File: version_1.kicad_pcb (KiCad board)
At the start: 2 copper layers, 98.6 x 99.9 mm, 145 parts, among them J1 motor_connector, J2 motor_connector, J3 motor_connector, J4 motor_connector, M5 Motor_Servo_JR, M6 Motor_Servo_JR, M7 Motor_Servo_JR, M8 Motor_Servo_JR, Q1 AO3400A, Q10 AO3400A, Q11 AO3400A, Q12 AO3400A, Q13 AO3400A, Q14 AO3400A, Q15 AO3400A, Q16 AO3400A, Q17 AO3401A, Q18 AO3401A, Q19 AO3401A, Q2 AO3400A, Q20 AO3401A, Q21 AO3400A, Q22 AO3400A, Q23 AO3400A, Q24 AO3400A, Q25 AO3400A, Q26 AO3400A, Q3 AO3400A, Q4 AO3400A, Q5 AO3400A, Q6 AO3400A, Q7 AO3400A, Q8 AO3400A, Q9 AO3400A, SW1 SW_SPDT, U1 Pico, U10 74AHC595, U11 ADP2302ARDZ-5.0, U12 LSM6DS3, U2 SLM2009, U3 SLM2009, U4 SLM2009, U5 SLM2009, U6 SLM2009, U7 SLM2009, U8 SLM2009, U9 SLM2009

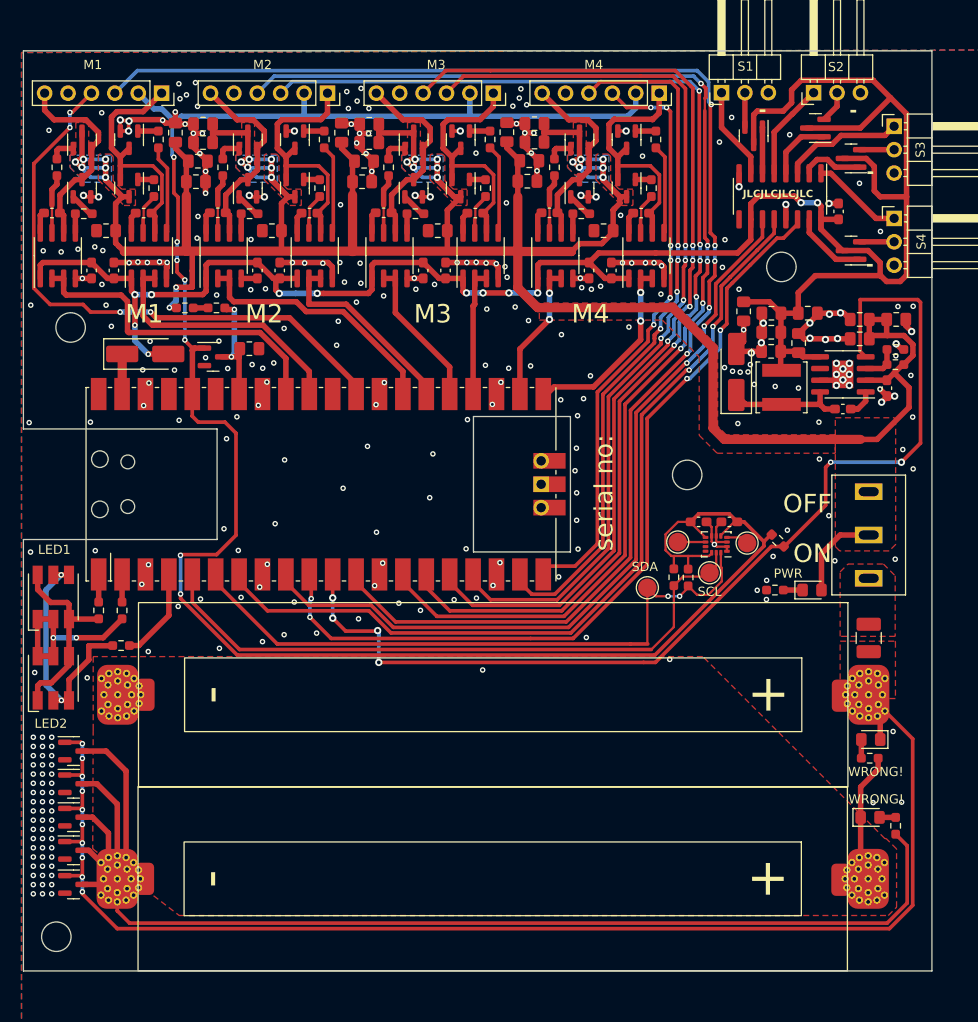
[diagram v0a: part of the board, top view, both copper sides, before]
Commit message: new version of layout with diodes improved power routing a little bit
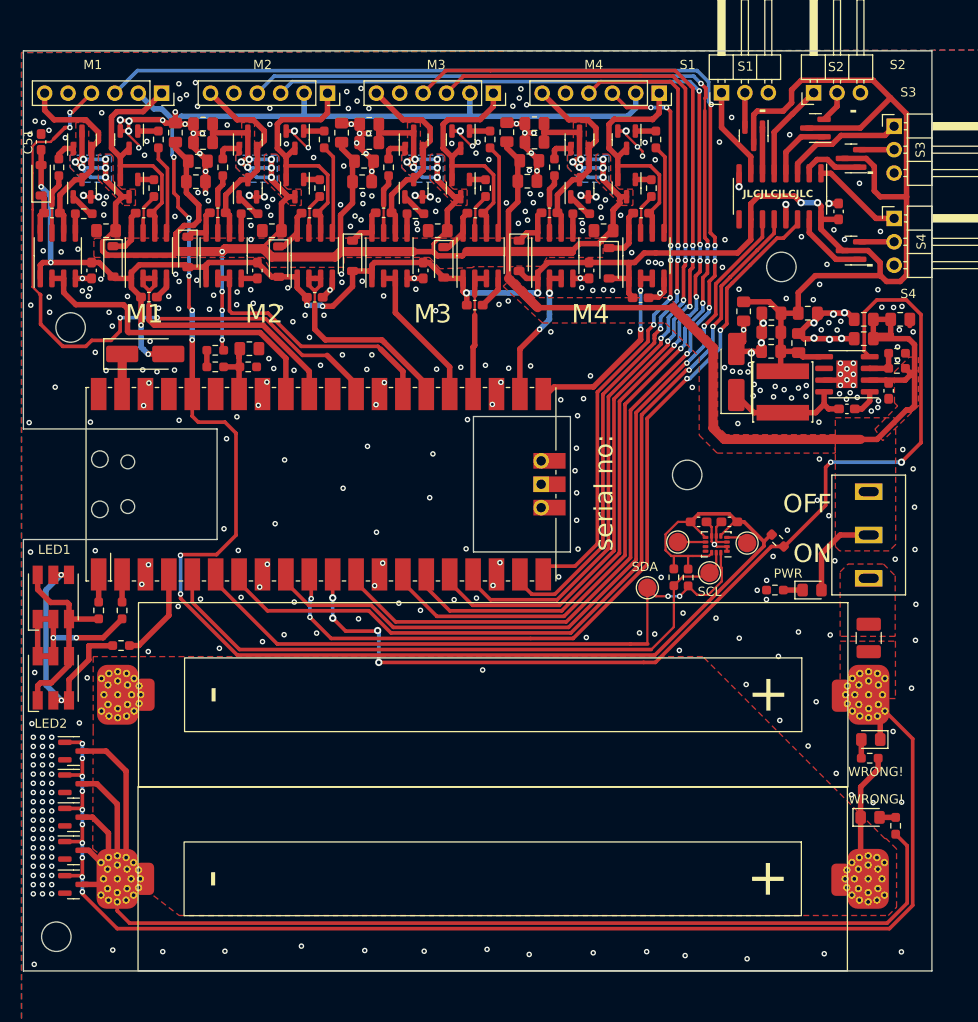
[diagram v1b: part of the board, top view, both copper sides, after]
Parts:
- removed Q26: AO3400A, Package_TO_SOT_SMD:SOT-23
- added C51: 100n, Capacitor_SMD:C_0603_1608Metric_Pad1.08x0.95mm_HandSolder, F.Cu at (25.6, 31.3)
- added D10: C8598, Diode_SMD:D_SOD-123, F.Cu at (77.4, 43.6)
- added D11: C8598, Diode_SMD:D_SOD-123, F.Cu at (25.6, 35.5)
- added D12: C8598, Diode_SMD:D_SOD-123, F.Cu at (51.3, 44.3)
- added D13: C8598, Diode_SMD:D_SOD-123, F.Cu at (69.2, 44.4)
- added D14: C8598, Diode_SMD:D_SOD-123, F.Cu at (87.2, 44.5)
- added D15: C8598, Diode_SMD:D_SOD-123, F.Cu at (33.4, 44.2)
- added D8: C8598, Diode_SMD:D_SOD-123, F.Cu at (41.5, 43.2)
- added D9: C8598, Diode_SMD:D_SOD-123, F.Cu at (59.4, 43.6)
- added R25: 1k, Resistor_SMD:R_0603_1608Metric_Pad0.98x0.95mm_HandSolder, F.Cu at (48.0, 55.7)
- L1: footprint Inductor_SMD:L_Changjiang_FNR5020S -> Inductor_SMD:L_Changjiang_FNR6045S
- moved R26 6.40 mm to (44.5, 55.7)
- moved R27 5.66 mm to (44.5, 53.9), turned to 180 degrees
- moved C22 4.92 mm to (72.6, 49.0), turned to 0 degrees
- moved C21 4.79 mm to (55.2, 48.1), turned to 0 degrees
- moved C24 4.78 mm to (37.2, 48.1), turned to 0 degrees
- moved C23 4.34 mm to (90.6, 48.2), turned to 0 degrees
- moved L1 0.52 mm to (106.0, 58.4)
- moved R18 0.44 mm to (118.5, 54.2)
- moved R19 0.44 mm to (118.5, 55.9)
- moved C13 0.44 mm to (118.8, 50.5)
- moved C30 0.44 mm to (114.8, 52.6)
- moved C31 0.44 mm to (114.8, 50.5)
- moved U11 0.44 mm to (113.0, 56.5)
- moved C9 0.44 mm to (113.0, 60.3)
- moved C14 0.34 mm to (117.5, 58.3)
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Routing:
- net VCC: track 409.0 -> 362.1 mm, vias 26 -> 28
- net +5V: track 232.6 -> 249.1 mm, vias 12 -> 10
- net GND: track 138.8 -> 125.4 mm, vias 305 -> 424
- net /ENCODER7: track 65.2 -> 71.7 mm
- net Net-(U1-GPIO28_ADC2): track 14.2 -> 7.66 mm, vias 2 -> 0
- net Net-(D14-K): track 2.33 -> 5.83 mm
- net Net-(D15-K): track 2.33 -> 5.37 mm
- net /MR1: track 22.3 -> 25.2 mm
- net Net-(D13-K): track 2.33 -> 5.07 mm
- net Net-(D12-K): track 2.33 -> 4.97 mm
- net Net-(D9-K): track 2.48 -> 4.93 mm
- net Net-(D10-K): track 2.48 -> 4.86 mm
- net Net-(D8-K): track 2.48 -> 4.63 mm
- net Net-(D11-K): track 2.48 -> 4.51 mm
- net /power/Pgood: track 114.8 -> 112.8 mm
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
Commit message: najnowsza wersja
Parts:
- removed D7: C2843868, LED_SMD:LED_RGB_5050-6
- U12: value LSM6DS3 -> C967633
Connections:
- D6 pad 1: Net-(D6-BA) -> GND
- D6 pad 2: Net-(D6-BK) -> GND
- D6 pad 3: Net-(D6-BK) -> GND
- D6 pad 6: Net-(D6-GA) -> Net-(D6-RA)
- R21 pad 1: Net-(D6-BA) -> Net-(D6-RA)
- R23 pad 1: Net-(D6-BK) -> Net-(D6-BA)
- R23 pad 2: Net-(U1-GPIO2) -> Net-(U1-GPIO4)
- U1 pad 4: Net-(U1-GPIO2) -> /SDA
- U1 pad 6: /SDA -> Net-(U1-GPIO4)
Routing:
- net Net-(D6-BK): track 27.8 -> 0.00 mm, vias 2 -> 0
- net Net-(U1-GPIO4): track 0.00 -> 17.7 mm, vias 0 -> 2
- net Net-(D6-BA): track 21.4 -> 5.21 mm
- net Net-(U1-GPIO2): track 11.0 -> 0.00 mm
- net Net-(D6-GA): track 19.8 -> 9.81 mm, vias 2 -> 0
- net Net-(D6-RA): track 0.00 -> 9.23 mm
- net /SDA: track 70.8 -> 78.7 mm, vias 2 -> 4
- net GND: vias 424 -> 431

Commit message: added moany componaets
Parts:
- added C11: 22u, Capacitor_SMD:C_0805_2012Metric_Pad1.18x1.45mm_HandSolder, F.Cu at (169.6, 102.1)
- added C32: 22u, Capacitor_SMD:C_0805_2012Metric_Pad1.18x1.45mm_HandSolder, F.Cu at (169.6, 105.1)
- added C33: 22u, Capacitor_SMD:C_0805_2012Metric_Pad1.18x1.45mm_HandSolder, F.Cu at (169.6, 108.1)
- added C34: 22u, Capacitor_SMD:C_0805_2012Metric_Pad1.18x1.45mm_HandSolder, F.Cu at (169.6, 111.1)
- added C35: 22u, Capacitor_SMD:C_0805_2012Metric_Pad1.18x1.45mm_HandSolder, F.Cu at (169.6, 114.1)
- added C40: 22u, Capacitor_SMD:C_0805_2012Metric_Pad1.18x1.45mm_HandSolder, F.Cu at (185.9, 102.1)
- added C41: 22u, Capacitor_SMD:C_0805_2012Metric_Pad1.18x1.45mm_HandSolder, F.Cu at (197.8, 91.5)
- added C42: 22u, Capacitor_SMD:C_0805_2012Metric_Pad1.18x1.45mm_HandSolder, F.Cu at (197.8, 94.5)
- added C43: 22u, Capacitor_SMD:C_0805_2012Metric_Pad1.18x1.45mm_HandSolder, F.Cu at (197.8, 97.5)
- added C44: 22u, Capacitor_SMD:C_0805_2012Metric_Pad1.18x1.45mm_HandSolder, F.Cu at (185.9, 114.1)
- added C45: 22u, Capacitor_SMD:C_0805_2012Metric_Pad1.18x1.45mm_HandSolder, F.Cu at (197.8, 71.5)
- added C46: 22u, Capacitor_SMD:C_0805_2012Metric_Pad1.18x1.45mm_HandSolder, F.Cu at (197.8, 74.5)
- added C47: 22u, Capacitor_SMD:C_0805_2012Metric_Pad1.18x1.45mm_HandSolder, F.Cu at (185.9, 91.1)
- added C48: 22u, Capacitor_SMD:C_0805_2012Metric_Pad1.18x1.45mm_HandSolder, F.Cu at (185.9, 94.1)
- added C49: 22u, Capacitor_SMD:C_0805_2012Metric_Pad1.18x1.45mm_HandSolder, F.Cu at (185.9, 97.1)
- added C52: 22u, Capacitor_SMD:C_0805_2012Metric_Pad1.18x1.45mm_HandSolder, F.Cu at (169.6, 85.1)
- added C53: 22u, Capacitor_SMD:C_0805_2012Metric_Pad1.18x1.45mm_HandSolder, F.Cu at (169.6, 88.1)
- added C54: 22u, Capacitor_SMD:C_0805_2012Metric_Pad1.18x1.45mm_HandSolder, F.Cu at (169.6, 91.1)
- added C55: 22u, Capacitor_SMD:C_0805_2012Metric_Pad1.18x1.45mm_HandSolder, F.Cu at (169.6, 94.1)
- added C56: 22u, Capacitor_SMD:C_0805_2012Metric_Pad1.18x1.45mm_HandSolder, F.Cu at (169.6, 97.1)
- added CN1: B6B-PH-K-S(LF)(SN), footprint:CONN-TH_B6B-PH-K-S, F.Cu at (190.0, 134.5)
- added CN2: B6B-PH-K-S(LF)(SN), footprint:CONN-TH_B6B-PH-K-S, F.Cu at (207.3, 134.5)
- added CN3: B6B-PH-K-S(LF)(SN), footprint:CONN-TH_B6B-PH-K-S, F.Cu at (172.7, 134.5)
- added CN4: B6B-PH-K-S(LF)(SN), footprint:CONN-TH_B6B-PH-K-S, F.Cu at (155.4, 134.5)
- added U13: DRV8870DDA, Package_SO:Texas_HTSOP-8-1EP_3.9x4.9mm_P1.27mm_EP2.95x4.9mm_Mask2.4x3.1mm_ThermalVias, F.Cu at (177.5, 70.5)
- added U14: BH-18650-B5BA016, footprint:BAT-SMD_BH-18650-B5BA016, F.Cu at (74.6, 111.3)
- added U15: DRV8870DDA, Package_SO:Texas_HTSOP-8-1EP_3.9x4.9mm_P1.27mm_EP2.95x4.9mm_Mask2.4x3.1mm_ThermalVias, F.Cu at (168.8, 58.3)
- added U16: DRV8870DDA, Package_SO:Texas_HTSOP-8-1EP_3.9x4.9mm_P1.27mm_EP2.95x4.9mm_Mask2.4x3.1mm_ThermalVias, F.Cu at (179.0, 47.6)
- added U17: DRV8870DDA, Package_SO:Texas_HTSOP-8-1EP_3.9x4.9mm_P1.27mm_EP2.95x4.9mm_Mask2.4x3.1mm_ThermalVias, F.Cu at (195.2, 57.3)
- R25: value 1k -> 10k
- R26: value 1k -> 33k
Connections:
- R26 pad 1: Net-(R26-Pad1) -> VCC
- U1 pad 11: /power/Pgood -> /ENCODER7
- U1 pad 29: /ENCODER7 -> /power/Pgood

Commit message: specified correct shift register
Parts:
- added C1: 100n, Capacitor_SMD:C_0603_1608Metric_Pad1.08x0.95mm_HandSolder, F.Cu at (160.8, 38.3)
- added C2: 100n, Capacitor_SMD:C_0603_1608Metric_Pad1.08x0.95mm_HandSolder, F.Cu at (132.7, 105.2)
- added C3: 100n, Capacitor_SMD:C_0603_1608Metric_Pad1.08x0.95mm_HandSolder, F.Cu at (160.8, 33.8)
- added C4: 100n, Capacitor_SMD:C_0603_1608Metric_Pad1.08x0.95mm_HandSolder, F.Cu at (160.8, 29.3)
- added D1: WRONG!, Diode_SMD:D_0805_2012Metric_Pad1.15x1.40mm_HandSolder, F.Cu at (133.0, 94.3)
- added D3: WRONG!, Diode_SMD:D_0805_2012Metric_Pad1.15x1.40mm_HandSolder, F.Cu at (133.0, 97.3)
- added D7: WRONG!, Diode_SMD:D_0805_2012Metric_Pad1.15x1.40mm_HandSolder, F.Cu at (133.0, 100.4)
- added F1: DFN, Fuse:Fuse_1210_3225Metric_Pad1.42x2.65mm_HandSolder, F.Cu at (142.7, 94.9)
- added R17: 1k, Resistor_SMD:R_0603_1608Metric_Pad0.98x0.95mm_HandSolder, F.Cu at (137.5, 94.0)
- added R20: 1k, Resistor_SMD:R_0603_1608Metric_Pad0.98x0.95mm_HandSolder, F.Cu at (137.5, 96.5)
- added R27: 1k, Resistor_SMD:R_0603_1608Metric_Pad0.98x0.95mm_HandSolder, F.Cu at (137.5, 99.1)
- added U18: SM04B-SRSS-TB_(LF)(SN), footprint:CONN-SMD_4P-P1.00_SM04B-SRSS-TB-LF-SN, F.Cu at (141.1, 59.4)
- added U2: SS-12D10L5, footprint:SW-TH_SS-12D10L5, F.Cu at (128.3, 73.3)
- M5, M6, M7, M8: footprint Connector_PinHeader_2.54mm:PinHeader_1x03_P2.54mm_Horizontal -> Connector_PinHeader_2.54mm:PinHeader_1x03_P2.54mm_Vertical
- moved U14 53.4 mm to (72.9, 164.6)
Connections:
- net /Untitled Sheet5/PWM renamed /Servo2/PWM
- net /Untitled Sheet5/PWR renamed /Servo2/PWR
- net /Untitled Sheet6/PWM renamed /Servo/PWM
- net /Untitled Sheet6/PWR renamed /Servo/PWR
- net /power/Pgood renamed /Power/Pgood
- CN1 pad 2: unconnected-(CN1-Pad2) -> GND
- CN1 pad 3: unconnected-(CN1-Pad3) -> /ENCODER1
- CN1 pad 4: unconnected-(CN1-Pad4) -> /ENCODER2
- CN2 pad 2: unconnected-(CN2-Pad2) -> GND
- CN2 pad 3: unconnected-(CN2-Pad3) -> /ENCODER3
- CN2 pad 4: unconnected-(CN2-Pad4) -> /ENCODER4
- CN3 pad 2: unconnected-(CN3-Pad2) -> GND
- CN3 pad 3: unconnected-(CN3-Pad3) -> /ENCODER5
- CN3 pad 4: unconnected-(CN3-Pad4) -> /ENCODER6
- CN4 pad 2: unconnected-(CN4-Pad2) -> GND
- CN4 pad 3: unconnected-(CN4-Pad3) -> /ENCODER7
- CN4 pad 4: unconnected-(CN4-Pad4) -> /ENCODER8
- Q21 pad 1: Net-(BT4-+) -> VCC
- Q21 pad 3: Net-(BT3--) -> Net-(D1-A)
- Q22 pad 1: Net-(BT4-+) -> VCC
- Q22 pad 3: Net-(BT3--) -> Net-(D1-A)
- Q23 pad 1: Net-(BT4-+) -> VCC
- Q23 pad 3: Net-(BT3--) -> Net-(D1-A)
- Q24 pad 1: Net-(BT4-+) -> VCC
- Q24 pad 3: Net-(BT3--) -> Net-(D1-A)
- Q25 pad 1: Net-(BT4-+) -> VCC
- Q25 pad 3: Net-(BT3--) -> Net-(D1-A)
- U14 pad 1: unconnected-(U14-Pad1) -> Net-(F1-Pad2)
- U14 pad 2: unconnected-(U14-Pad2) -> Net-(D7-A)
- U14 pad 3: unconnected-(U14-Pad3) -> Net-(D7-A)
- U14 pad 4: unconnected-(U14-Pad4) -> Net-(D3-A)
- U14 pad 5: unconnected-(U14-Pad5) -> Net-(D3-A)
- U14 pad 6: unconnected-(U14-Pad6) -> Net-(D1-A)
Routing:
- net /Power/Pgood: track 112.8 -> 0.00 mm, vias 6 -> 0
- net /ENCODER7: track 71.7 -> 184.5 mm, vias 4 -> 10
- net VCC: vias 28 -> 38
- net Net-(BT4-+): vias 10 -> 0
- removed copper zone on F.Cu, net Net-(BT4-+)

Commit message: big layout changes
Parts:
- removed BT3, BT4: Battery_Cell, 18650:single
- removed the C1 at (62.7, 39.0)
- removed C10, C12, C17, C18, C19, C20, C34 (x2), C35 (x2), C43 (x2), C44 (x2), C48 (x2), C49 (x2), C55, C56: 22u, Capacitor_SMD:C_0805_2012Metric_Pad1.18x1.45mm_HandSolder
- removed the C11 at (42.6, 33.4)
- removed the C2 at (72.7, 39.0)
- removed C21, C22, C23, C24, C9: 100n, Capacitor_SMD:C_0603_1608Metric_Pad1.08x0.95mm_HandSolder
- removed the C3 at (44.7, 39.0)
- removed the C32 at (40.1, 30.3)
- removed the C33 at (43.1, 29.4)
- removed the C4 at (54.7, 39.0)
- removed the C40 at (78.5, 33.3)
- removed the C41 at (76.1, 30.2)
- removed the C42 at (79.1, 29.3)
- removed the C45 at (60.6, 33.4)
- removed the C46 at (58.2, 30.3)
- removed the C47 at (61.2, 29.4)
- removed the D1 at (115.5, 104.6)
- removed the D1 at (133.0, 94.3)
- removed D10, D11, D12, D13, D14, D15, D8, D9: C8598, Diode_SMD:D_SOD-123
- removed D2: C145232, Diode_SMD:D_SMA_Handsoldering
- removed the D3 at (115.6, 96.2)
- removed the F1 at (115.4, 85.1)
- removed J1, J2, J3, J4: motor_connector, Connector_PinSocket_2.54mm:PinSocket_1x06_P2.54mm_Vertical
- removed L1: L, Inductor_SMD:L_Changjiang_FNR6045S
- removed Q1, Q10, Q11, Q12, Q13, Q14, Q15, Q16, Q2, Q3, Q4, Q5, Q6, Q7, Q8, Q9: AO3400A, Package_TO_SOT_SMD:SOT-23
- removed R10, R11, R12, R13, R14, R15, R16, R5, R6, R7, R8, R9: 10, Resistor_SMD:R_0603_1608Metric_Pad0.98x0.95mm_HandSolder
- removed the R17 at (115.5, 98.2)
- removed R18, R28: 1k, Resistor_SMD:R_0603_1608Metric_Pad0.98x0.95mm_HandSolder
- removed R19, R24: 4k, Resistor_SMD:R_0603_1608Metric_Pad0.98x0.95mm_HandSolder
- removed the R20 at (118.3, 105.5)
- removed the R27 at (44.5, 53.9)
- removed SW1: SW_SPDT, switches:TSM1x3
- removed TP1, TP2: TestPoint, TestPoint:TestPoint_Pad_D2.0mm
- removed TP3: SDA, TestPoint:TestPoint_Pad_D2.0mm
- removed TP4: SCL, TestPoint:TestPoint_Pad_D2.0mm
- removed U11: ADP2302ARDZ-5.0, Package_SO:SOIC-8-1EP_3.9x4.9mm_P1.27mm_EP2.29x3mm
- removed U14: BH-18650-B5BA016, footprint:BAT-SMD_BH-18650-B5BA016
- removed the U2 at (63.4, 43.6)
- removed U7, U8, U9: SLM2009, Package_SO:SOIC-8_3.9x4.9mm_P1.27mm
- added C57: 22u, Capacitor_SMD:C_0805_2012Metric_Pad1.18x1.45mm_HandSolder, F.Cu at (156.5, 101.1)
- added C58: 22u, Capacitor_SMD:C_0805_2012Metric_Pad1.18x1.45mm_HandSolder, F.Cu at (156.5, 104.1)
- added C59: 22u, Capacitor_SMD:C_0805_2012Metric_Pad1.18x1.45mm_HandSolder, F.Cu at (194.1, 94.3)
- added C60: 100n, Capacitor_SMD:C_0603_1608Metric_Pad1.08x0.95mm_HandSolder, F.Cu at (163.6, 90.0)
- added C61: 100n, Capacitor_SMD:C_0603_1608Metric_Pad1.08x0.95mm_HandSolder, F.Cu at (163.6, 92.5)
- added D1: WRONG!, Diode_SMD:D_0805_2012Metric_Pad1.15x1.40mm_HandSolder, F.Cu at (116.9, 138.6)
- added JP1: Jumper_3_Bridged12, Jumper:SolderJumper-3_P1.3mm_Bridged12_RoundedPad1.0x1.5mm, F.Cu at (19.4, 48.6)
- added JP2: Jumper_3_Bridged12, Jumper:SolderJumper-3_P1.3mm_Bridged12_RoundedPad1.0x1.5mm, F.Cu at (24.7, 32.6)
- added JP3: Jumper_3_Bridged12, Jumper:SolderJumper-3_P1.3mm_Bridged12_RoundedPad1.0x1.5mm, F.Cu at (24.7, 35.9)
- added JP4: Jumper_3_Bridged12, Jumper:SolderJumper-3_P1.3mm_Bridged12_RoundedPad1.0x1.5mm, F.Cu at (47.4, 47.6)
- C6: value 100n -> 330n
- C8: value 100n -> 22u; footprint Capacitor_SMD:C_0603_1608Metric_Pad1.08x0.95mm_HandSolder -> Capacitor_SMD:C_0805_2012Metric_Pad1.18x1.45mm_HandSolder
- R1: value 10 -> 1k
- R17, R20, R27: value 1k -> 220
- R2: value 10 -> 56k
- R3, R4: value 10 -> 10k
- U10: value 74AHC595 -> 74HCT595D
- U3: value SLM2009 -> L7805CD2T-TR; footprint Package_SO:SOIC-8_3.9x4.9mm_P1.27mm -> footprint:TO-263-2_L10.0-W9.1-P5.08-LS15.2-TL
- U4: value SLM2009 -> TPS562209DDCR; footprint Package_SO:SOIC-8_3.9x4.9mm_P1.27mm -> footprint:SOT-23-6_L2.9-W1.6-P0.95-LS2.8-BL
- U5: value SLM2009 -> FXL0530-4R7-M; footprint Package_SO:SOIC-8_3.9x4.9mm_P1.27mm -> footprint:IND-SMD_L5.4-W5.2_FXL0530
- U6: value SLM2009 -> BH-18650-B5BA016; footprint Package_SO:SOIC-8_3.9x4.9mm_P1.27mm -> footprint:BAT-SMD_BH-18650-B5BA016
- moved CN2 178.6 mm to (66.9, 24.1), turned to 180 degrees
- moved C8 164.8 mm to (193.6, 89.4), turned to 0 degrees
- moved CN3 163.6 mm to (51.9, 24.3), turned to 180 degrees
- moved CN4 162.1 mm to (36.7, 24.1), turned to 180 degrees
- moved C7 161.0 mm to (172.0, 108.3), turned to -90 degrees
- moved U17 160.7 mm to (36.1, 34.7), turned to 90 degrees
- moved CN1 154.3 mm to (82.3, 24.1), turned to 180 degrees
- moved C46 145.8 mm to (57.0, 36.7)
- moved C45 145.8 mm to (57.0, 33.7)
- moved U4 140.3 mm to (168.7, 110.5), turned to -90 degrees
- moved C47 138.8 mm to (57.0, 39.7)
- moved C52 137.9 mm to (41.7, 33.6)
- moved C53 137.9 mm to (41.7, 36.6)
- moved C54 137.9 mm to (41.7, 39.6)
- moved C41 137.3 mm to (72.0, 36.6)
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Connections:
- C5 pad 1: Net-(D10-K) -> Linear 5V
- C5 pad 2: Net-(J3-Pin_6) -> GND
- C6 pad 1: Net-(J3-Pin_1) -> VCC
- C6 pad 2: Net-(D14-K) -> GND
- C7 pad 1: Net-(D11-K) -> Net-(U4-SW)
- C7 pad 2: Net-(J4-Pin_6) -> Net-(U4-VBST)
- C8 pad 1: Net-(J4-Pin_1) -> +5V
- C8 pad 2: Net-(D15-K) -> GND
- CN1 pad 2: GND -> ENC_PWR_G
- CN1 pad 5: +3.3V -> ENC_PWR_P
- CN2 pad 2: GND -> ENC_PWR_G
- CN2 pad 5: +3.3V -> ENC_PWR_P
- CN3 pad 2: GND -> ENC_PWR_G
- CN3 pad 5: +3.3V -> ENC_PWR_P
- CN4 pad 2: GND -> ENC_PWR_G
- CN4 pad 5: +3.3V -> ENC_PWR_P
- D3 pad 2: Net-(D3-A) -> 1S
- D5 pad 2: +5V -> Net-(D5-A)
- F1 pad 1: Net-(SW1-C) -> Net-(F1-Pad1)
- R1 pad 1: Net-(U2-HO) -> GND
- R1 pad 2: Net-(Q1-G) -> Net-(D4-K)
- R2 pad 1: Net-(U2-LO) -> Net-(U4-VFB)
- R2 pad 2: Net-(Q2-G) -> Net-(JP4-A)
- R20 pad 2: Net-(D3-A) -> 1S
- R3 pad 1: Net-(U3-HO) -> GND
- R3 pad 2: Net-(Q3-G) -> Net-(U4-VFB)
- R4 pad 1: Net-(U3-LO) -> Net-(U4-EN)
- R4 pad 2: Net-(Q4-G) -> VCC
- U1 pad 29: /Power/Pgood -> unconnected-(U1-GPIO22-Pad29)
- U12 pad 4: Net-(U12-INT1) -> unconnected-(U12-INT1-Pad4)
- U12 pad 9: Net-(U12-INT2) -> unconnected-(U12-INT2-Pad9)
- U2 pad 1: unconnected-(U2-Pad1) -> Net-(F1-Pad1)
- U2 pad 2: unconnected-(U2-Pad2) -> VCC
- U3 pad 1: +5V -> VCC
- U3 pad 3: /MR2 -> Linear 5V
- U4 pad 1: +5V -> GND
- U4 pad 2: /ML1 -> Net-(U4-SW)
- U4 pad 3: /ML1 -> VCC
- U4 pad 4: GND -> Net-(U4-VFB)
- U4 pad 5: Net-(U4-LO) -> Net-(U4-EN)
- U4 pad 6: Net-(J1-Pin_6) -> Net-(U4-VBST)
- U5 pad 1: +5V -> Net-(U4-SW)
- U5 pad 2: /MR1 -> Net-(JP4-A)
- U6 pad 1: +5V -> Net-(D7-A)
- U6 pad 2: /ML3 -> Net-(F1-Pad2)
- U6 pad 3: /ML3 -> 1S
- U6 pad 4: GND -> Net-(D7-A)
- U6 pad 5: Net-(U6-LO) -> Net-(D1-A)
- U6 pad 6: Net-(J3-Pin_6) -> 1S
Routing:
- net VCC: track 362.1 -> 120.0 mm, vias 38 -> 10
- net +5V: track 249.1 -> 37.6 mm, vias 10 -> 2
- net /ENCODER7: track 184.5 -> 16.0 mm, vias 10 -> 2
- net Net-(BT4-+): track 149.1 -> 0.00 mm
- net +3.3V: track 223.8 -> 80.8 mm, vias 7 -> 2
- net /ENCODER8: track 158.0 -> 16.5 mm, vias 5 -> 2
- net Net-(BT3--): track 134.4 -> 0.00 mm
- net Net-(D1-A): track 1.75 -> 120.3 mm
- net 1S: track 0.00 -> 109.0 mm
- net /ENCODER2: track 127.5 -> 18.9 mm, vias 5 -> 2
- net Net-(D7-A): track 0.00 -> 105.3 mm
- net /ENCODER1: track 134.7 -> 32.1 mm, vias 5 -> 4
- net ENC_PWR_P: track 0.00 -> 88.3 mm, vias 0 -> 7
- net ENC_PWR_G: track 0.00 -> 82.0 mm, vias 0 -> 1
- net /ENCODER3: track 108.1 -> 32.1 mm
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- added copper zone on F.Cu, net (none)
- added copper zone on F.Cu, net Net-(F1-Pad1)
- removed copper zone on F.Cu, net Net-(BT3-+)
- removed copper zone on F.Cu, net Net-(SW1-C)
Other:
- board size 98.6 x 99.9 mm -> 100 x 120 mm
- board text removed: "-"
- board text removed: "JLCJLCJLCJLC"

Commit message: clean up
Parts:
- moved U3 51.1 mm to (84.5, 72.7), turned to -90 degrees
- moved JP4 49.8 mm to (97.0, 51.0)
- moved C14 44.4 mm to (143.8, 71.1)
- moved C59 44.4 mm to (173.5, 55.0)
- moved R3 44.4 mm to (158.5, 71.0)
- moved R4 44.4 mm to (153.9, 69.7)
- moved C5 44.4 mm to (159.9, 41.1)
- moved C60 44.4 mm to (143.0, 50.6)
- moved C13 44.4 mm to (141.2, 82.3)
- moved C30 44.4 mm to (141.2, 86.1)
- moved C31 44.4 mm to (141.7, 71.1)
- moved C57 44.4 mm to (135.9, 61.7)
- moved C58 44.4 mm to (135.9, 64.7)
- moved C7 44.4 mm to (151.4, 69.0)
- moved C8 44.4 mm to (173.0, 50.0)
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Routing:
- net /SCL: track 15.7 -> 45.6 mm, vias 0 -> 2
- net /SDA: track 17.0 -> 39.1 mm, vias 2 -> 0
- net +3.3V: track 80.8 -> 96.5 mm
- net GND: track 141.2 -> 149.2 mm, vias 34 -> 37
- net Net-(D5-A): track 11.4 -> 6.43 mm
- net Net-(D6-GA): track 8.16 -> 3.40 mm
- net VCC: track 120.0 -> 115.3 mm
- net Net-(D6-RA): track 7.58 -> 3.29 mm
- net Net-(D1-A): track 120.3 -> 123.5 mm
- net Net-(U1-GPIO4): track 16.0 -> 13.2 mm
